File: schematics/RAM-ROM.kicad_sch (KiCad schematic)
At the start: 7 parts, among them U10 2764, U9 SIMM16M

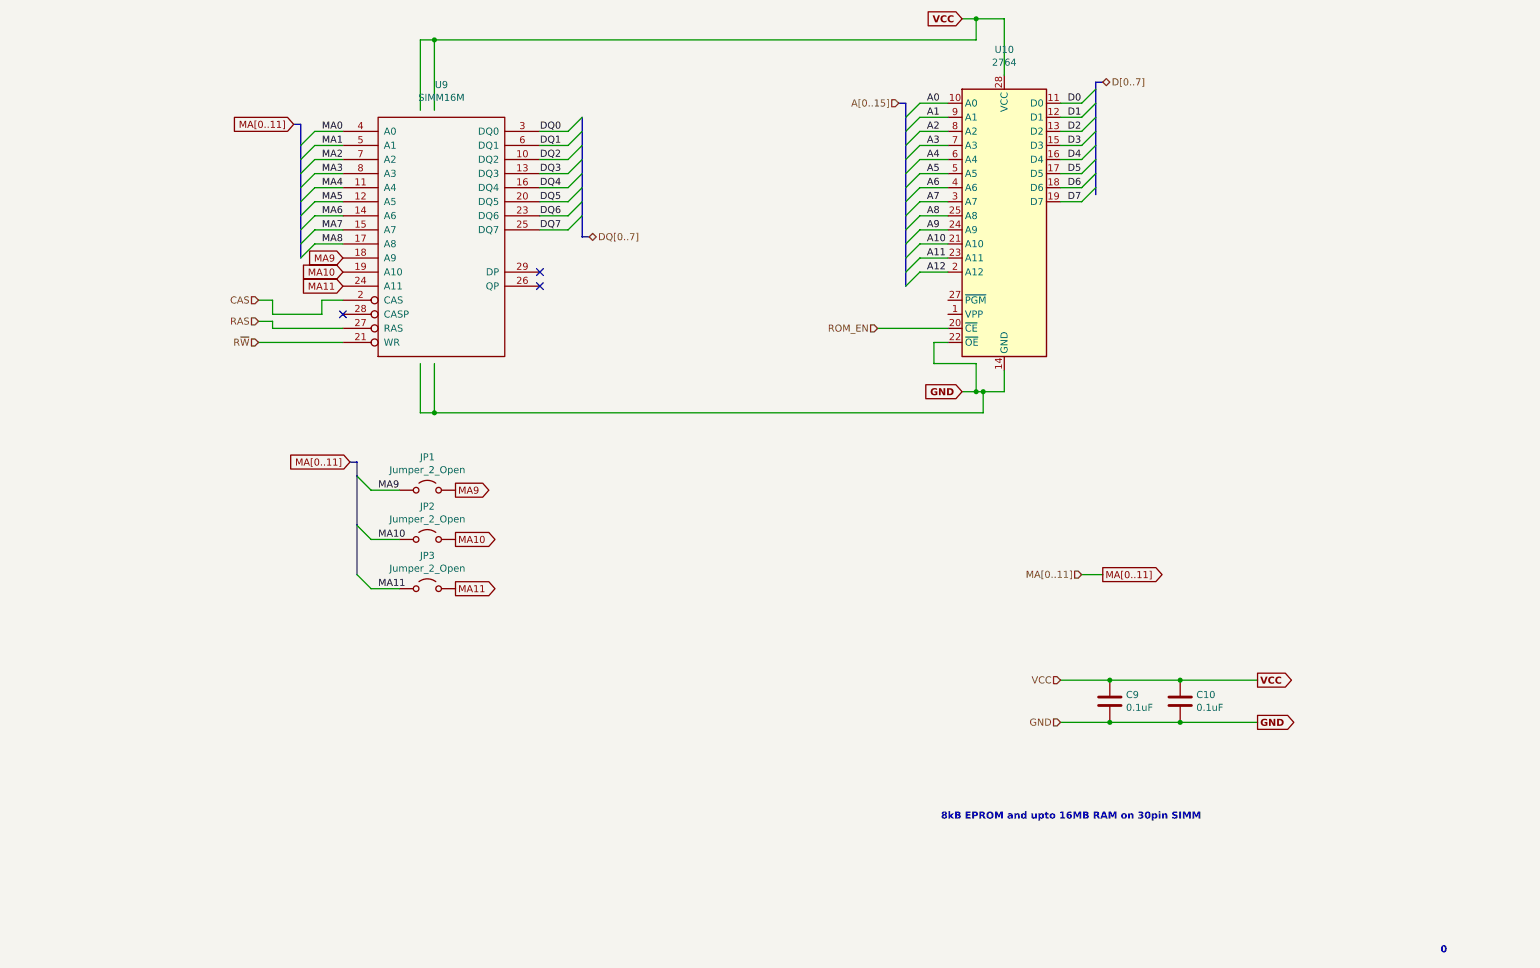
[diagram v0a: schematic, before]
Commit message: Small tweaks here and there. Added a lot of missing footprint definitions.
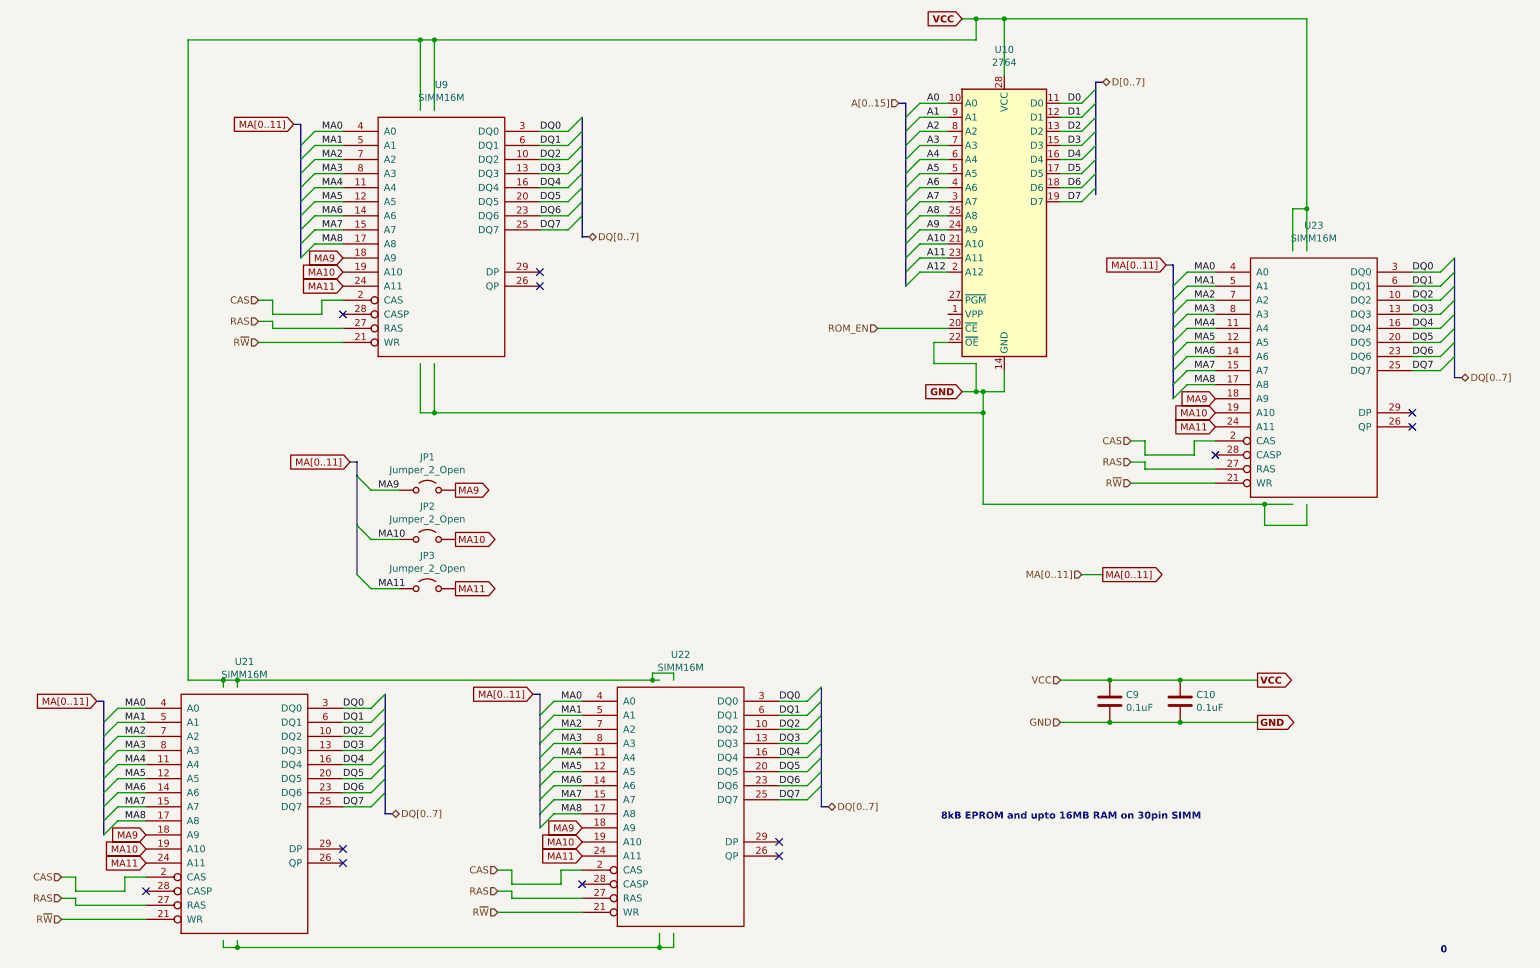
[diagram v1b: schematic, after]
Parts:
- added U21, U22, U23: SIMM16M, Custom_Socket:SIMM, symbol simm16m:SIMM16M
- C10, C9: footprint (none) -> Capacitor_THT:CP_Radial_D4.0mm_P1.50mm
- U9: footprint (none) -> Custom_Socket:SIMM
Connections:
- net CAS: now also U21.2 (CAS), U22.2 (CAS), U23.2 (CAS)
- net DQ0: now also U21.3 (DQ0), U22.3 (DQ0), U23.3 (DQ0)
- net DQ1: now also U21.6 (DQ1), U22.6 (DQ1), U23.6 (DQ1)
- net DQ2: now also U21.10 (DQ2), U22.10 (DQ2), U23.10 (DQ2)
- net DQ3: now also U21.13 (DQ3), U22.13 (DQ3), U23.13 (DQ3)
- net DQ4: now also U21.16 (DQ4), U22.16 (DQ4), U23.16 (DQ4)
- net DQ5: now also U21.20 (DQ5), U22.20 (DQ5), U23.20 (DQ5)
- net DQ6: now also U21.23 (DQ6), U22.23 (DQ6), U23.23 (DQ6)
- net DQ7: now also U21.25 (DQ7), U22.25 (DQ7), U23.25 (DQ7)
- net GND: now also U21.22 (GND), U21.9 (GND), U22.22 (GND), U22.9 (GND), U23.22 (GND), U23.9 (GND)
- net MA0: now also U21.4 (A0), U22.4 (A0), U23.4 (A0)
- net MA1: now also U21.5 (A1), U22.5 (A1), U23.5 (A1)
- net MA10: now also U21.19 (A10), U22.19 (A10), U23.19 (A10)
- net MA11: now also U21.24 (A11), U22.24 (A11), U23.24 (A11)
- net MA2: now also U21.7 (A2), U22.7 (A2), U23.7 (A2)
- net MA3: now also U21.8 (A3), U22.8 (A3), U23.8 (A3)
- net MA4: now also U21.11 (A4), U22.11 (A4), U23.11 (A4)
- net MA5: now also U21.12 (A5), U22.12 (A5), U23.12 (A5)
- net MA6: now also U21.14 (A6), U22.14 (A6), U23.14 (A6)
- net MA7: now also U21.15 (A7), U22.15 (A7), U23.15 (A7)
- net MA8: now also U21.17 (A8), U22.17 (A8), U23.17 (A8)
- net MA9: now also U21.18 (A9), U22.18 (A9), U23.18 (A9)
- net RAS: now also U21.27 (RAS), U22.27 (RAS), U23.27 (RAS)
- net R~{W}: now also U21.21 (WR), U22.21 (WR), U23.21 (WR)
- net VCC: now also U21.1 (VCC), U21.30 (VCC), U22.1 (VCC), U22.30 (VCC), U23.1 (VCC), U23.30 (VCC)
- no-connect marks 3 -> 12
